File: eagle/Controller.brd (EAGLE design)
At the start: 99.1 x 69.8 mm, 43 parts, among them Q1 IRF530N, Q2 IRF530N, Q3 IRF530N, Q4 IRF530N, Q5 IRF530N, Q6 IRF530N, U1 BC337

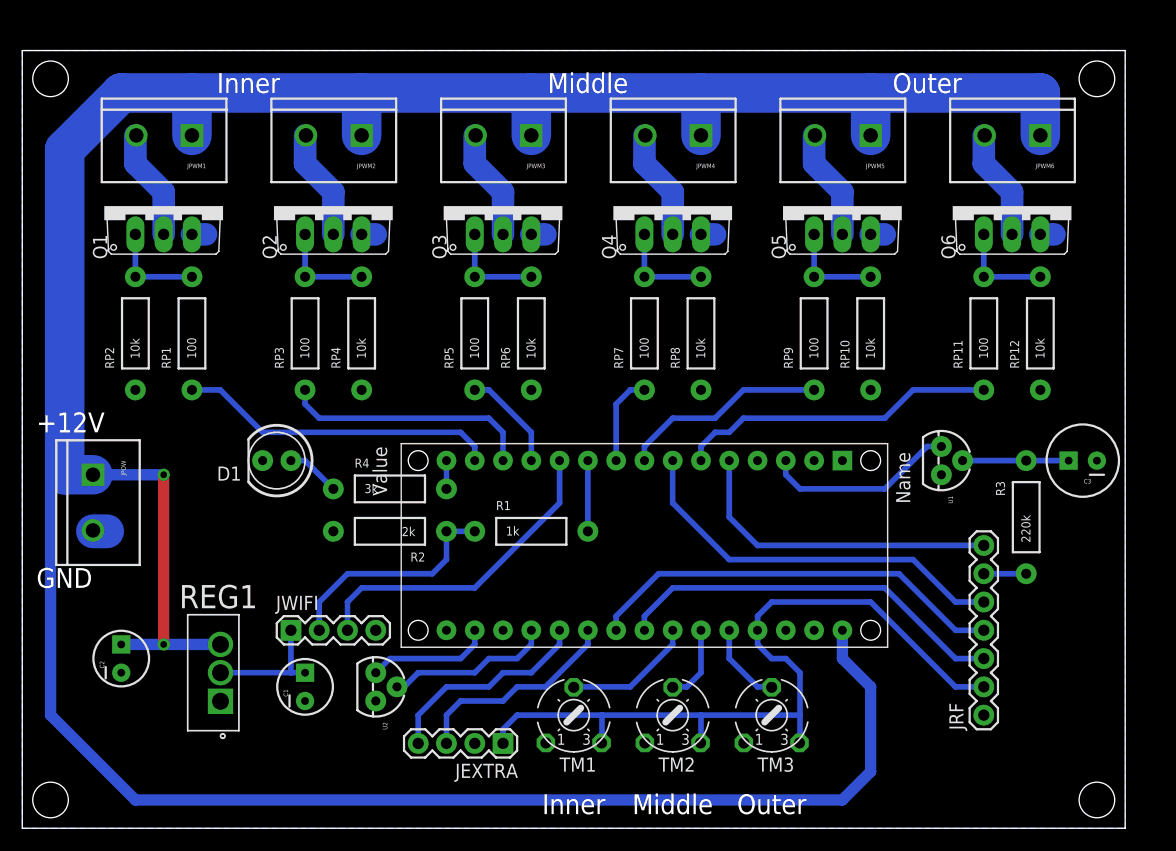
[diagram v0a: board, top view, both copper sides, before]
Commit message: Update board
Remove 2 trim pots and replace with EXTRA2/3
Increase size of vias
Increase border of board
Improve labeling
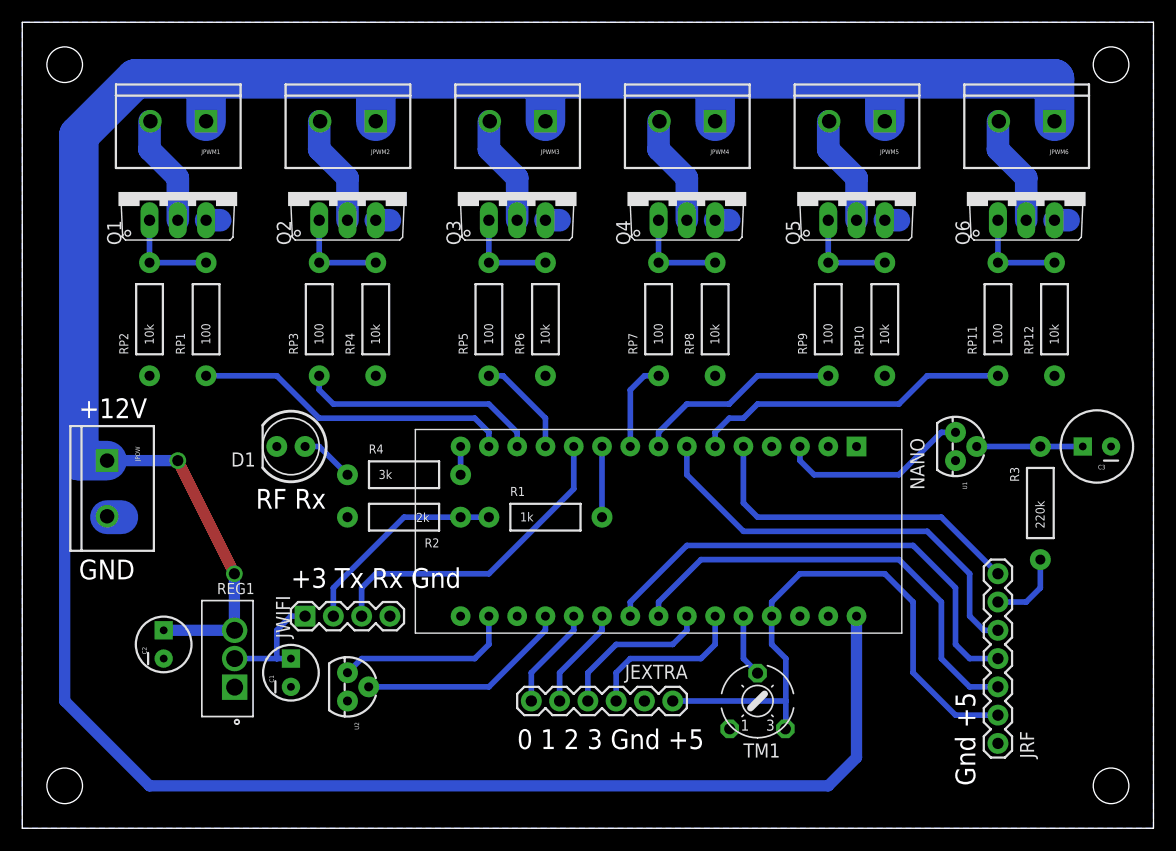
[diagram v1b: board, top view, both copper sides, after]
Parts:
- removed TM2, TM3: (no value), adafruit:6MM
- JEXTRA: device SparkFun-Connectors:1X04 -> SparkFun-Connectors:1X06
- NANO: value ARDUINONANO -> (none); device jet-lib:PDIP-32 -> jet-lib:PDIP-32-NO-MOUNT
- moved TM1 16.6 mm to (66.0, 11.4)
- moved JEXTRA 15.7 mm to (58.4, 11.4)
- moved C2 4.02 mm to (12.7, 16.5)
- moved JRF 2.84 mm to (87.6, 7.62)
- moved U2 2.54 mm to (29.2, 12.7)
- moved JPWM3 1.80 mm to (47.0, 63.5)
- moved Q5 1.80 mm to (74.9, 57.1)
- moved JPWM1 1.80 mm to (16.5, 63.5)
- moved JPOW 1.80 mm to (7.62, 33.0)
- moved JPWM2 1.80 mm to (31.8, 63.5)
- moved R1 1.80 mm to (47.0, 27.9)
- moved C1 1.80 mm to (24.1, 14.0)
- moved JPWM4 1.80 mm to (62.2, 63.5)
- moved JPWM5 1.80 mm to (77.5, 63.5)
- moved JPWM6 1.80 mm to (92.7, 63.5)
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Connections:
- removed net N$2: NANO.A1, TM2.S
- removed net N$3: NANO.A2, TM1.S
- new net EXTRA0: JEXTRA.6, NANO.A6
- new net EXTRA3: JEXTRA.3, NANO.A1
- net 5V: no longer TM2.E, TM3.E
- net EXTRA1: now also JEXTRA.5; no longer JEXTRA.3
- net EXTRA2: now also NANO.A2; no longer NANO.A6
- net GND: no longer TM2.A, TM3.A
- net N$1: now also TM1.S; no longer TM3.S
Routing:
- net 5V: track 71.3 -> 52.5 mm
- net EXTRA3: track 0.00 -> 15.0 mm
- net N$3: track 11.7 -> 0.00 mm
- net EXTRA1: track 19.1 -> 9.20 mm
- net EXTRA0: track 0.00 -> 9.20 mm
- net N$2: track 6.88 -> 0.00 mm
- net DAT1: track 38.0 -> 43.6 mm
- net DAT0: track 35.4 -> 41.0 mm
- net N$23: track 11.2 -> 16.3 mm
- net VIN: track 288.0 -> 283.1 mm
- net EXTRA2: track 19.1 -> 14.3 mm
- net N$20: track 15.5 -> 19.9 mm
- net N$5: track 3.81 -> 6.88 mm
- net DAT2: track 35.4 -> 38.5 mm
- net N$1: track 7.40 -> 5.61 mm
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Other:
- board size 99.1 x 69.8 mm -> 101.6 x 72.4 mm
- board text added: "+3 Tx Rx Gnd"
- board text added: "0 1 2 3 Gnd +5"
- board text added: "Gnd +5"
- board text added: "RF Rx"
- board text removed: "Inner"
- board text removed: "Middle"
- board text removed: "Outer"

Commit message: Add Revision to board
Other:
- board text added: ">CREVISION"
- board text added: "Rev:"
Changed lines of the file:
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@@
 <text x="24.13" y="21.59" size="1.778" layer="46">+3 Tx Rx Gnd</text>
 <text x="44.45" y="8.89" size="1.778" layer="46" align="top-left">0 1 2 3 Gnd +5</text>
+<text x="7.62" y="1.27" size="1.778" layer="46">Rev:</text>
+<text x="13.97" y="1.27" size="1.778" layer="46">&gt;CREVISION</text>
 </plain>
 <attributes>
+<attribute name="CREVISION" value="0.1"/>
 </attributes>
 <variantdefs>
@@
 <wire x1="16.51" y1="63.5" x2="16.51" y2="67.31" width="3.556" layer="16"/>
 <wire x1="12.7" y1="17.78" x2="19.05" y2="17.78" width="1.016" layer="16"/>
-<wire x1="16.51" y1="17.78" x2="19.05" y2="17.78" width="0" layer="19" extent="1-16"/>
 <wire x1="13.97" y1="33.02" x2="19.05" y2="22.86" width="1.016" layer="1"/>
-<wire x1="19.05" y1="22.86" x2="15.24" y2="22.86" width="0" layer="19" extent="1-16"/>
-<wire x1="15.24" y1="22.86" x2="15.24" y2="20.32" width="0" layer="19" extent="1-16"/>
-<wire x1="15.24" y1="20.32" x2="16.51" y2="19.05" width="0" layer="19" extent="1-16"/>
-<wire x1="16.51" y1="19.05" x2="16.51" y2="17.78" width="0" layer="19" extent="1-16"/>
+<wire x1="19.05" y1="17.78" x2="19.05" y2="22.86" width="1.016" layer="16"/>
 <wire x1="19.05" y1="17.78" x2="19.0754" y2="17.78" width="0" layer="19" extent="16-16"/>
 <wire x1="3.81" y1="33.02" x2="5.08" y2="33.02" width="0" layer="19" extent="16-16"/>
-<wire x1="19.05" y1="17.78" x2="19.05" y2="22.86" width="1.016" layer="16"/>
 </signal>
 <signal name="RESET">
